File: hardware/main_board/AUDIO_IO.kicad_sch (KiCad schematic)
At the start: 8 parts, among them IC2 LM4890M_NOPB, J10 Conn_01x04_Pin, J9 AudioJack

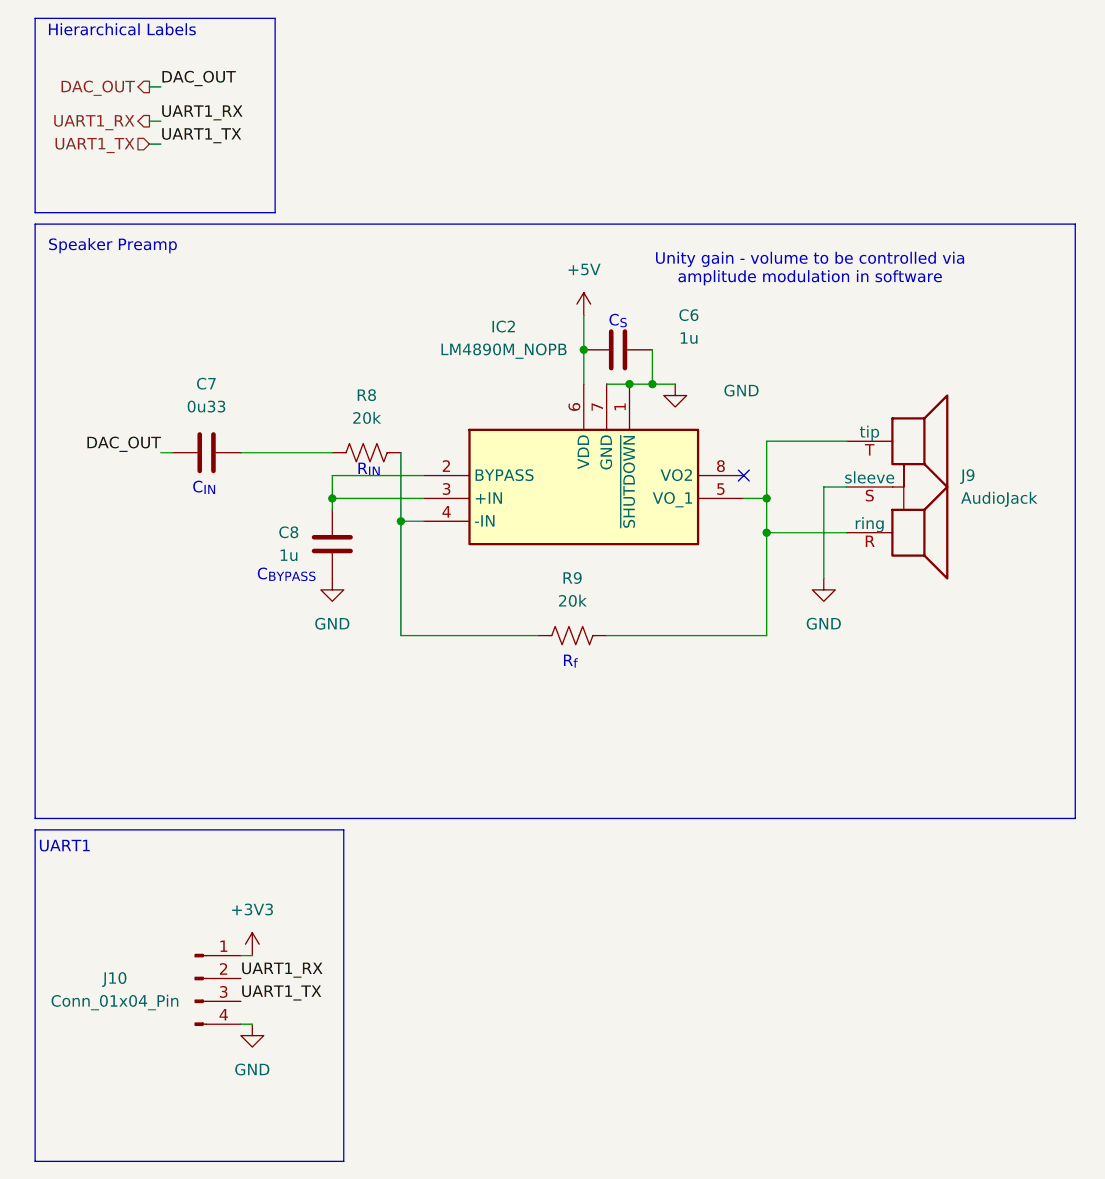
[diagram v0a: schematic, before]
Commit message: main board stuff. removed usbc for power. added level shifter for led logic signal. added lights for mux select signals. finished layout + pass DRC
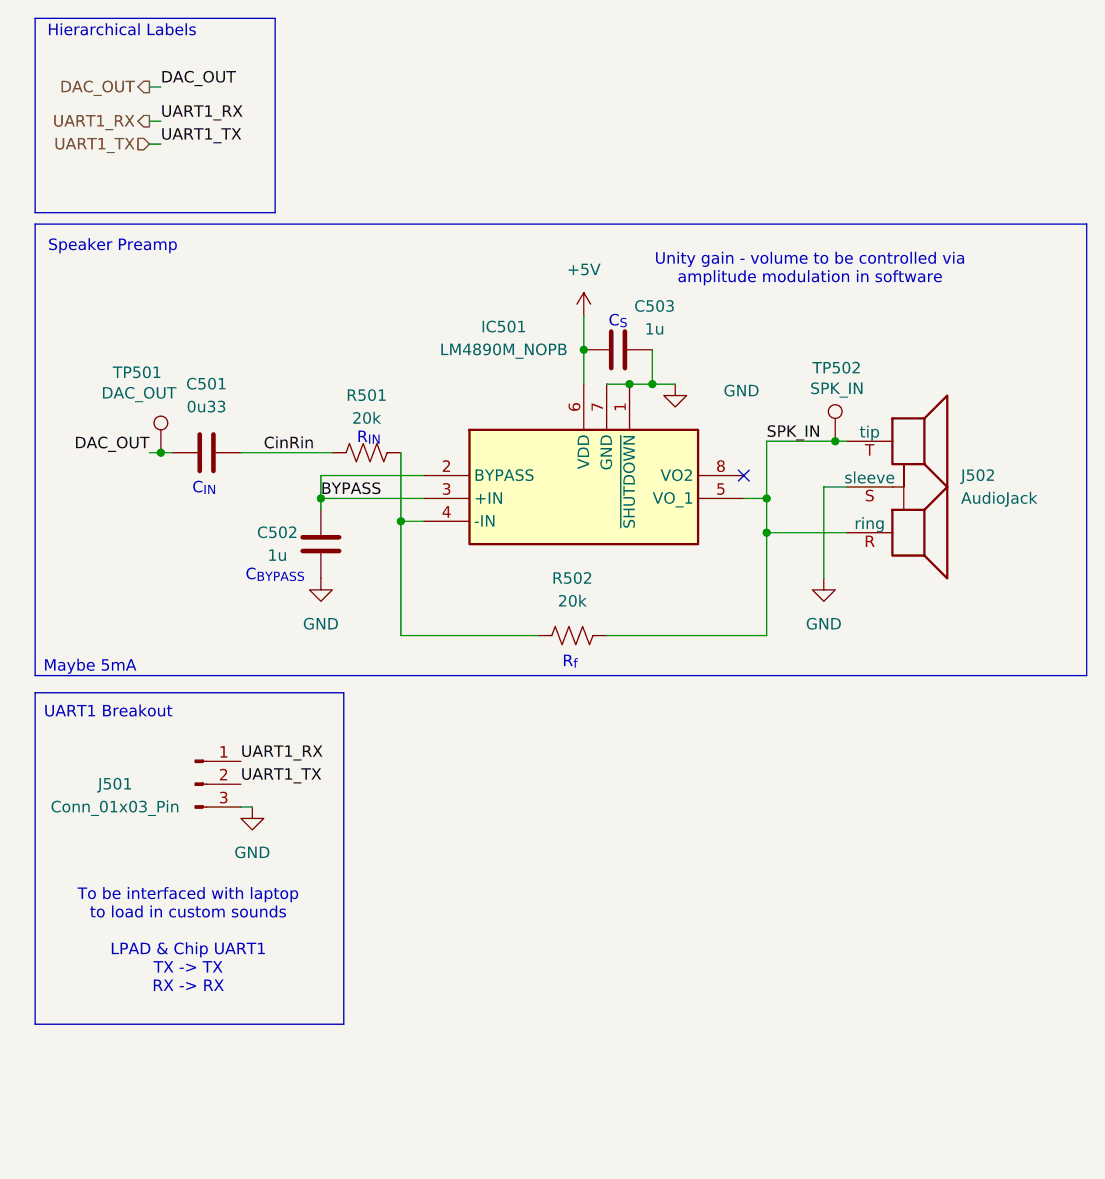
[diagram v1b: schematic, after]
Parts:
- added TP501: DAC_OUT, SamacSys_Parts:bettertestpoint2, symbol Connector:TestPoint
- added TP502: SPK_IN, SamacSys_Parts:bettertestpoint2, symbol Connector:TestPoint
- J501: renamed from J10; value Conn_01x04_Pin -> Conn_01x03_Pin; footprint Connector_PinHeader_2.54mm:PinHeader_1x05_P2.54mm_Vertical -> Connector_PinHeader_2.54mm:PinHeader_1x03_P2.54mm_Vertical; symbol Connector:Conn_01x04_Pin -> Connector:Conn_01x03_Pin
- renumbered C7 to C501, C8 to C502, C6 to C503, IC2 to IC501, J9 to J502, R8 to R501, R9 to R502
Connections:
- net +3V3 is gone; now on net UART1_RX: J501.1 (Pin_1)
- net DAC_OUT: now also TP501.1
- net GND: now also J501.3 (Pin_3); no longer J501.4 (Pin_4)
- net UART1_RX: no longer J501.2 (Pin_2)
- net UART1_TX: now also J501.2 (Pin_2); no longer J501.3 (Pin_3)
- net CinRin: now reaches C501.2, R501.1
- net BYPASS: now reaches C502.1, IC501.2 (BYPASS), IC501.3 (+IN)
- net SPK_IN: now reaches IC501.5 (VO_1), J502.R (ring), J502.T (tip), R502.2
- net SPK_IN: now also TP502.1
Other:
- note added: "Maybe 5mA"
- note added: "To be interfaced with laptop to load in custom sounds LPAD & Chip UART1 TX -> TX RX -> RX"
- note added: "UART1 Breakout"
- note removed: "UART1"
- moved on the sheet: C502

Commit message: bom
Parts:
- J501: now left out of the parts list
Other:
- note added: "10 mA"
- note removed: "Maybe 5mA"
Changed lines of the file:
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@@
 		)
 	)
-	(text "Maybe 5mA"
-		(exclude_from_sim no)
-		(at 20.066 86.106 0)
+	(text "10 mA"
+		(exclude_from_sim no)
+		(at 17.78 85.598 0)
 		(effects
 			(font
@@
 		(unit 1)
 		(exclude_from_sim no)
-		(in_bom yes)
+		(in_bom no)
 		(on_board yes)
 		(dnp no)
